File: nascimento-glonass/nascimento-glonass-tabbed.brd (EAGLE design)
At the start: 70 x 70 mm, 1 part, among them X1 BU-SMA-V

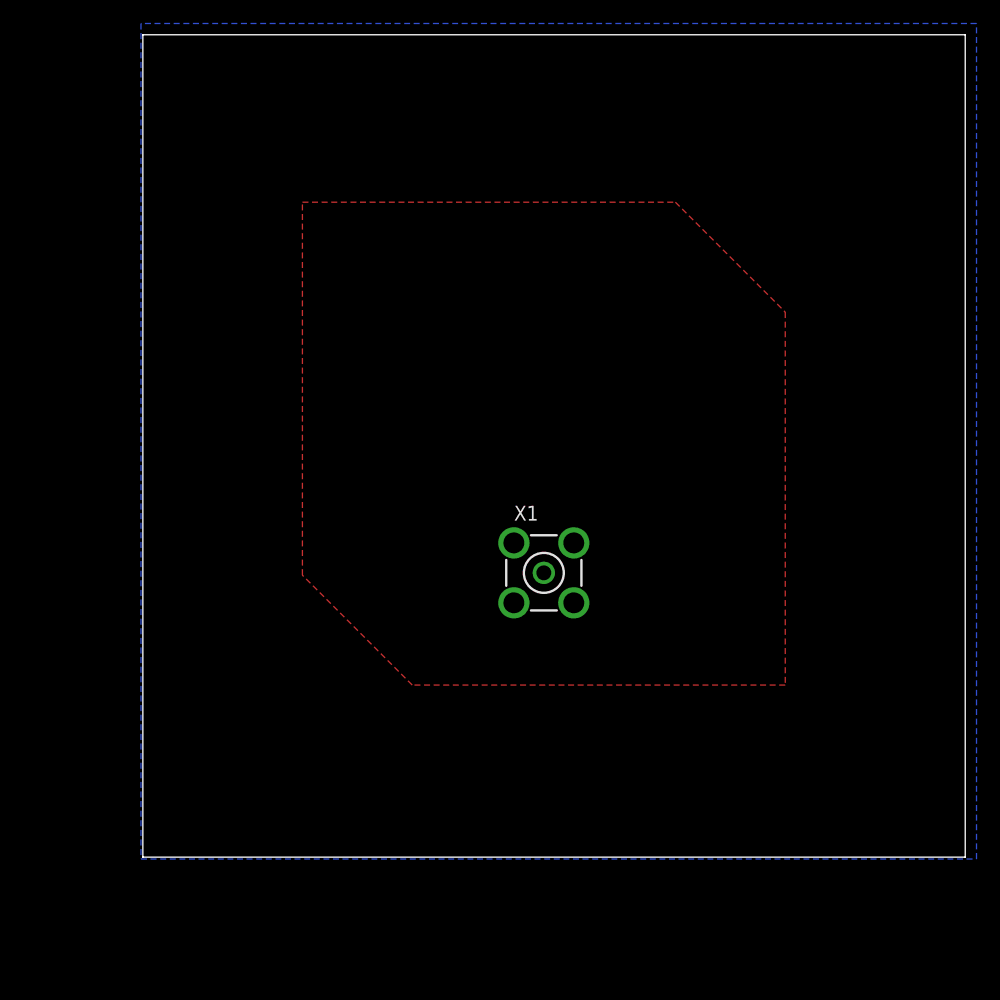
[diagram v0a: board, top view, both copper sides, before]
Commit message: Finished untabbed version. Unsure about ground plane.
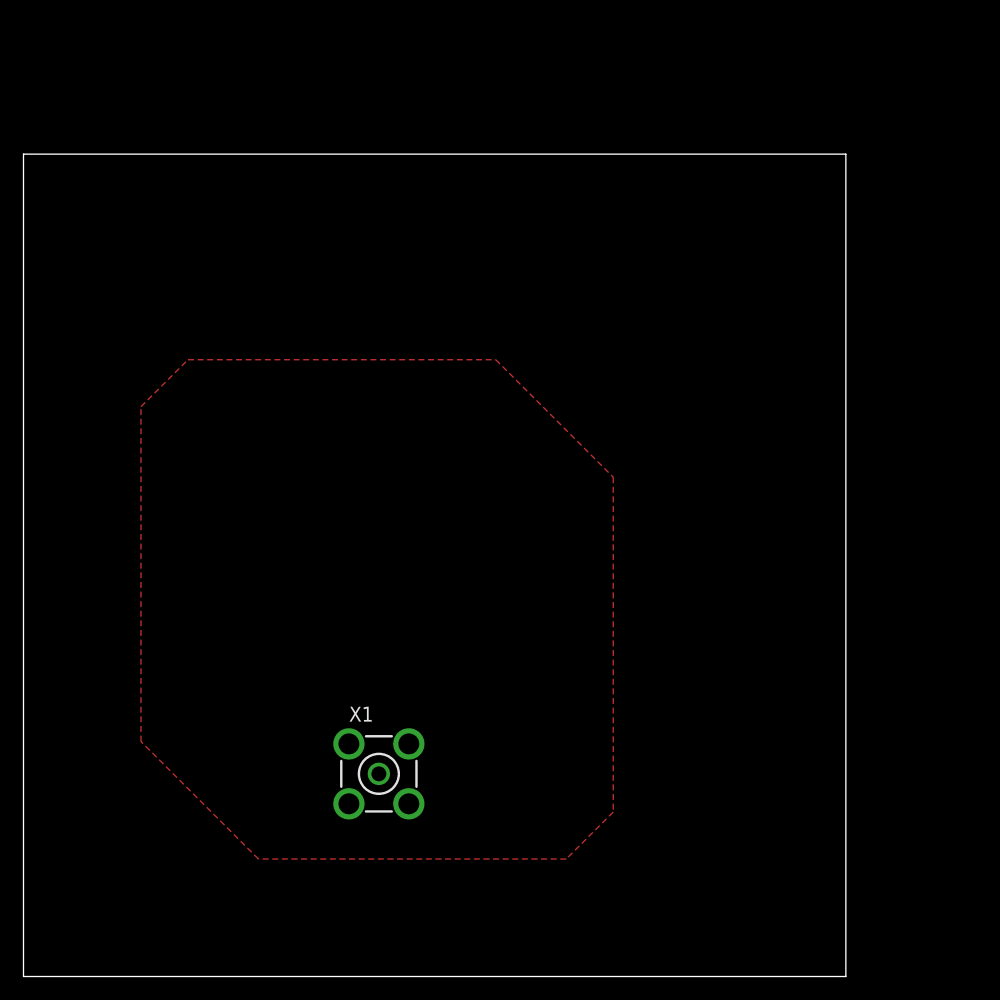
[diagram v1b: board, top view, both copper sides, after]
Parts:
- moved X1 22.1 mm to (20.2, 7.25)
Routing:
- added copper zone on layer 1, net N$1
- removed copper zone on layer 1, net ANTENNA
- removed copper zone on layer 16, net GND
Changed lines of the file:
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@@
 <setting verticaltext="up"/>
 </settings>
-<grid distance="0.1" unitdist="inch" unit="mm" style="dots" multiple="1" display="yes" altdistance="0.001" altunitdist="inch" altunit="inch"/>
+<grid distance="0.1" unitdist="mm" unit="mm" style="dots" multiple="1" display="yes" altdistance="0.001" altunitdist="inch" altunit="inch"/>
 <layers>
 <layer number="1" name="Top" color="4" fill="1" visible="yes" active="yes"/>
@@
 <layer number="14" name="Route14" color="1" fill="6" visible="no" active="no"/>
 <layer number="15" name="Route15" color="4" fill="6" visible="no" active="no"/>
-<layer number="16" name="Bottom" color="1" fill="1" visible="no" active="yes"/>
+<layer number="16" name="Bottom" color="1" fill="1" visible="yes" active="yes"/>
 <layer number="17" name="Pads" color="2" fill="1" visible="yes" active="yes"/>
 <layer number="18" name="Vias" color="2" fill="1" visible="yes" active="yes"/>
@@
 <board>
 <plain>
-<wire x1="0.16" y1="0.16" x2="70.16" y2="0.16" width="0" layer="20"/>
-<wire x1="70.16" y1="0.16" x2="70.16" y2="70.16" width="0" layer="20"/>
-<wire x1="70.16" y1="70.16" x2="0.16" y2="70.16" width="0" layer="20"/>
-<wire x1="0.16" y1="70.16" x2="0.16" y2="0.16" width="0" layer="20"/>
+<wire x1="-10" y1="-10" x2="60" y2="-10" width="0" layer="20"/>
+<wire x1="60" y1="-10" x2="60" y2="60" width="0" layer="20"/>
+<wire x1="60" y1="60" x2="-10" y2="60" width="0" layer="20"/>
+<wire x1="-10" y1="60" x2="-10" y2="-10" width="0" layer="20"/>
 </plain>
 <attributes>
@@
 </autorouter>
 <elements>
-<element name="X1" library="con-coax" package="BU-SMA-V" value="BU-SMA-V" x="34.2914" y="24.3582">
-<attribute name="OC_NEWARK" value="unknown" x="34.2914" y="24.3582" size="1.778" layer="27" display="off"/>
-<attribute name="MPN" value="" x="34.2914" y="24.3582" size="1.778" layer="27" display="off"/>
-<attribute name="MF" value="" x="34.2914" y="24.3582" size="1.778" layer="27" display="off"/>
-<attribute name="OC_FARNELL" value="unknown" x="34.2914" y="24.3582" size="1.778" layer="27" display="off"/>
+<element name="X1" library="con-coax" package="BU-SMA-V" value="BU-SMA-V" x="20.25" y="7.25">
+<attribute name="OC_NEWARK" value="unknown" x="20.25" y="7.25" size="1.778" layer="27" display="off"/>
+<attribute name="MPN" value="" x="20.25" y="7.25" size="1.778" layer="27" display="off"/>
+<attribute name="MF" value="" x="20.25" y="7.25" size="1.778" layer="27" display="off"/>
+<attribute name="OC_FARNELL" value="unknown" x="20.25" y="7.25" size="1.778" layer="27" display="off"/>
 </element>
 </elements>
@@
 <contactref element="X1" pad="5"/>
 <contactref element="X1" pad="2"/>
-<polygon width="0.3302" layer="16" thermals="no" rank="5">
-<vertex x="71.12" y="71.12"/>
-<vertex x="0" y="71.12"/>
-<vertex x="0" y="0"/>
-<vertex x="71.12" y="0"/>
-</polygon>
+<wire x1="22.7999" y1="4.7001" x2="22.7999" y2="9.7999" width="0" layer="19" extent="1-1"/>
+<wire x1="17.7001" y1="9.7999" x2="22.7999" y2="9.7999" width="0" layer="19" extent="1-1"/>
+<wire x1="17.7001" y1="4.7001" x2="22.7999" y2="4.7001" width="0" layer="19" extent="1-1"/>
 </signal>
 <signal name="ANTENNA">
 <contactref element="X1" pad="1"/>
-<polygon width="0.33" layer="1" isolate="0.1" thermals="no">
-<vertex x="23.0914" y="14.8082"/>
-<vertex x="13.7414" y="24.1582"/>
-<vertex x="13.7414" y="55.9082"/>
-<vertex x="45.4914" y="55.9082"/>
-<vertex x="54.8414" y="46.5582"/>
-<vertex x="54.8414" y="14.8082"/>
+</signal>
+<signal name="N$1">
+<polygon width="0.1" layer="1">
+<vertex x="10" y="0"/>
+<vertex x="0" y="10"/>
+<vertex x="0" y="38.5"/>
+<vertex x="4" y="42.5"/>
+<vertex x="30.2" y="42.5"/>
+<vertex x="40.2" y="32.5"/>
+<vertex x="40.2" y="4"/>
+<vertex x="36.2" y="0"/>
 </polygon>
 </signal>
